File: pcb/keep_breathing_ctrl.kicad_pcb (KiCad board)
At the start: 4 copper layers, 131 x 112 mm, 177 parts, among them J2 Screw_Terminal, P1 CONN_RASPBERRY, Q1 PN2222, Q2 PN2222, U1 MPL3115A2, U10 PCF8523TK, U11 AQH3213AX, U12 AQH3213AX, U13 HTS221, U14 ICE40UP5K-SG48ITR, U15 GD25Q32CTIGR-Memory_Flash, U16 UCC12040, U17 ISO7762, U18 ZLDO1117G33TA, U19 NCP177, U2 powerSTEP01, U3 TLP240D, U4 TLP240D, U5 TLP240D, U6 TLP240D, U7 TLP240D, U8 TLP240D, U9 ZLDO1117G33TA, Y1 ABS06-107-32.768KHZ-T

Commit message: fix
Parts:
- moved C65 9.49 mm to (157.5, 103.0), turned to 180 degrees
- moved C67 3.77 mm to (157.5, 105.5), turned to 180 degrees
- moved C56 3.71 mm to (104.0, 107.0)
- moved C22 3.42 mm to (82.0, 114.0)
- moved C14 2.99 mm to (80.0, 121.5)
- moved C66 1.28 mm to (138.0, 107.0), turned to 180 degrees
- moved C64 0.89 mm to (134.0, 107.0)
- moved C57 0.46 mm to (108.0, 107.0), turned to 180 degrees
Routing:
- net +5V: track 83.5 -> 100.4 mm
- net +3V3: track 38.5 -> 48.5 mm

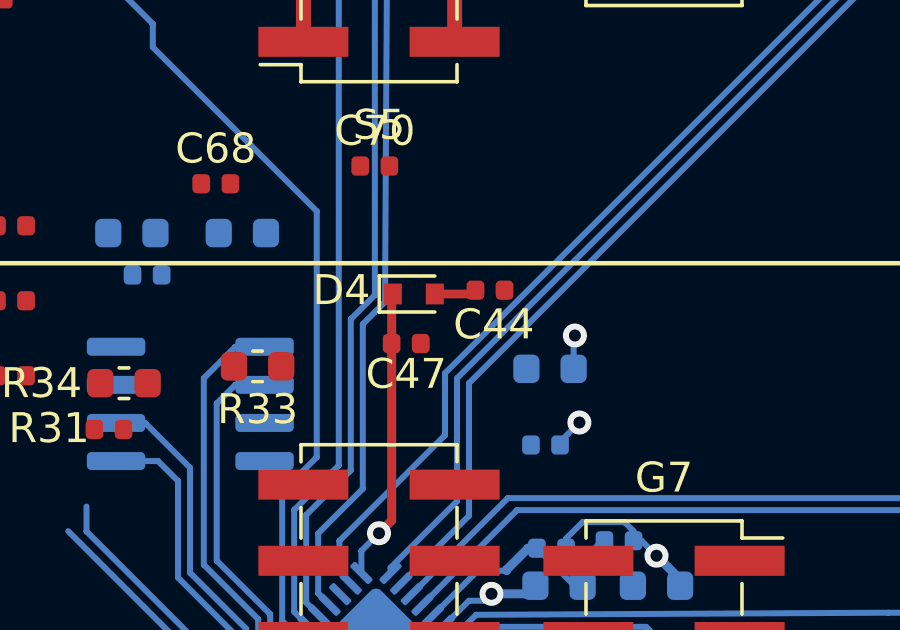
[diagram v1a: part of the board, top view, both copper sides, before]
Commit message: footprint fix
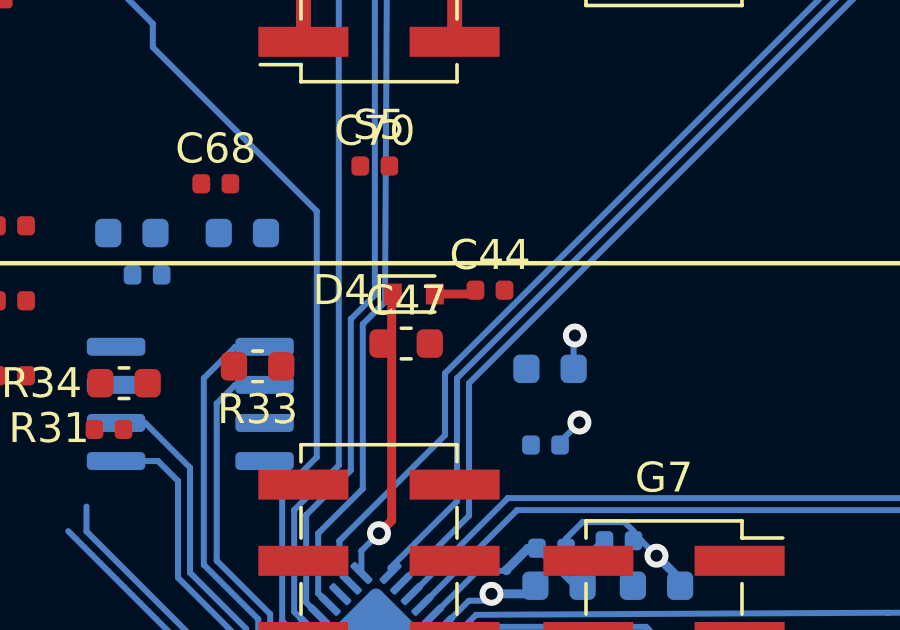
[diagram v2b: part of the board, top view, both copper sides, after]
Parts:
- C42, C44: footprint Resistor_SMD:R_0402_1005Metric -> Capacitor_SMD:C_0402_1005Metric
- C47: footprint Resistor_SMD:R_0402_1005Metric -> Capacitor_SMD:C_0603_1608Metric

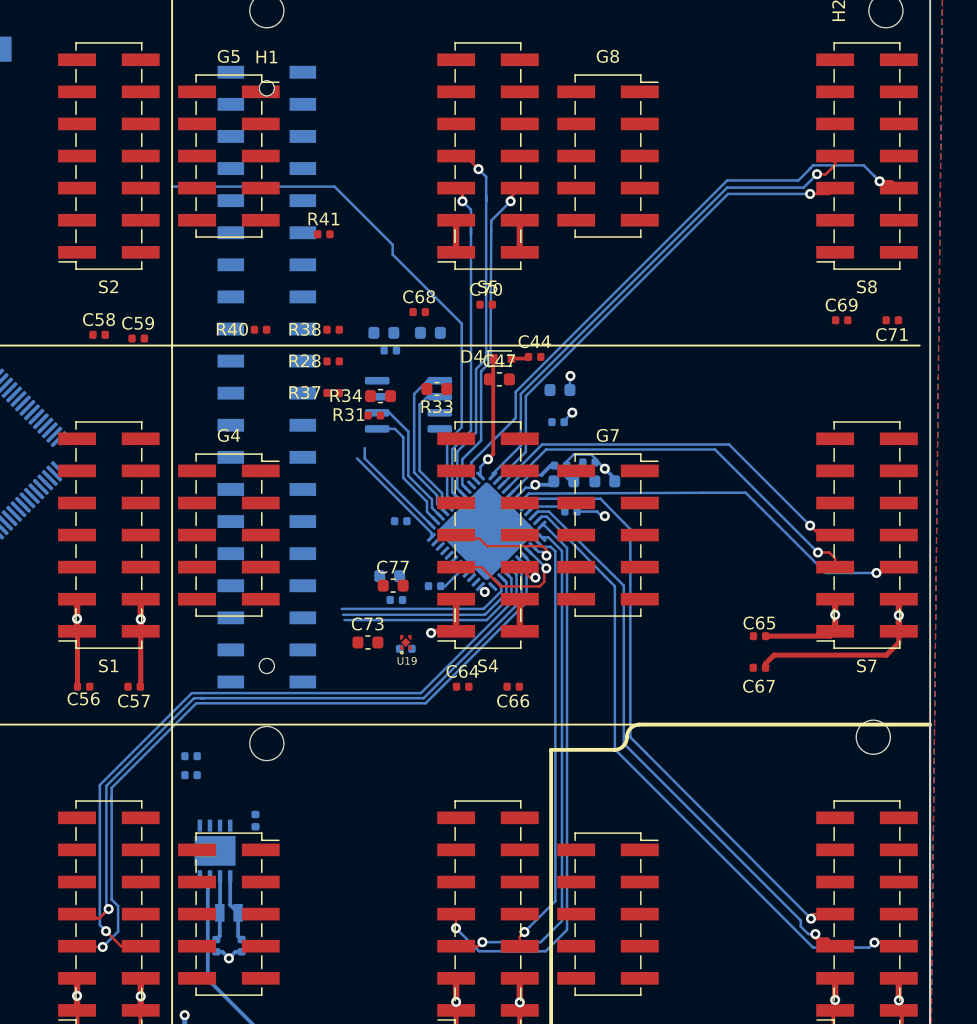
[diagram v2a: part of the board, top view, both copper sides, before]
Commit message: SPI for sensor shield array
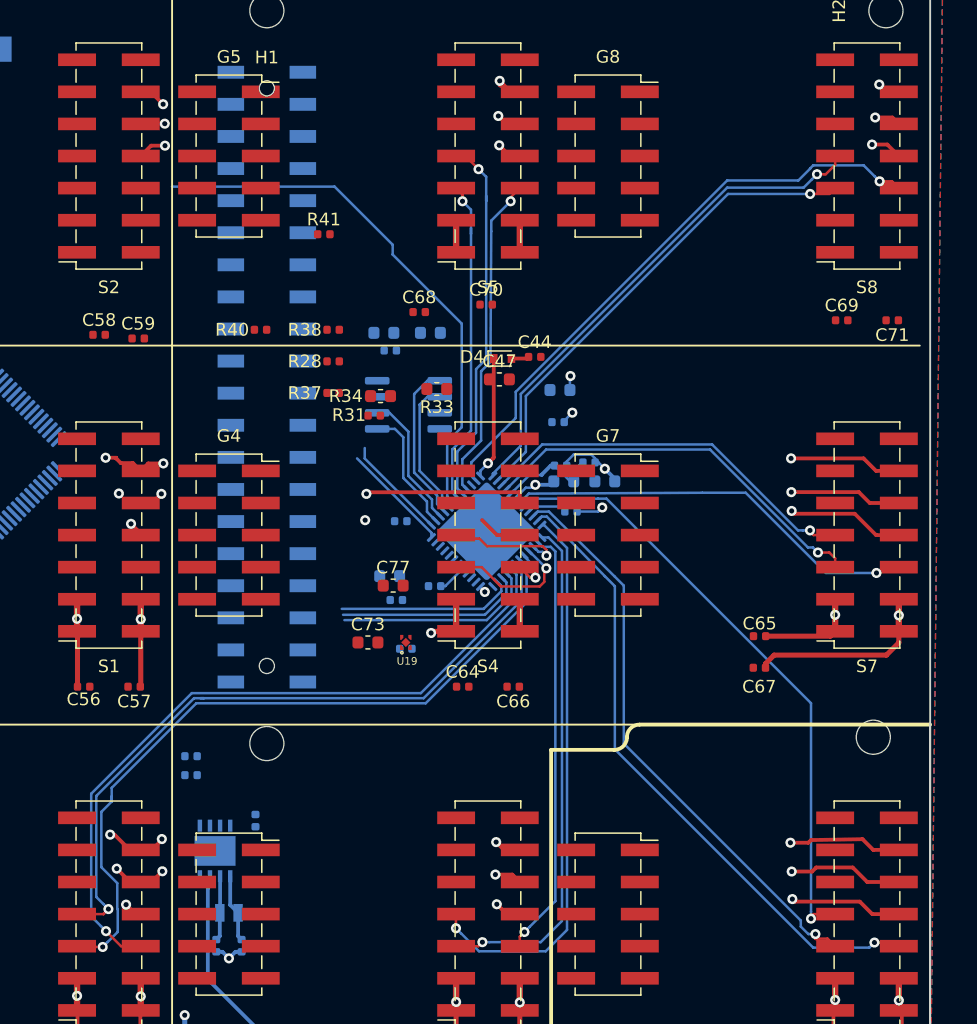
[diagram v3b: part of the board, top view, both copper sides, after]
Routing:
- net /SensorShields/SPI_MISO: track 0.00 -> 263.9 mm, vias 0 -> 11
- net /SensorShields/SPI_CLK: track 0.00 -> 256.8 mm, vias 0 -> 9
- net /SensorShields/SPI_MOSI: track 0.00 -> 254.5 mm, vias 0 -> 10
- net /SensorShields/I2C_CLK_0: track 58.3 -> 59.0 mm
- net /SensorShields/SPI_CS_0: track 56.6 -> 57.2 mm

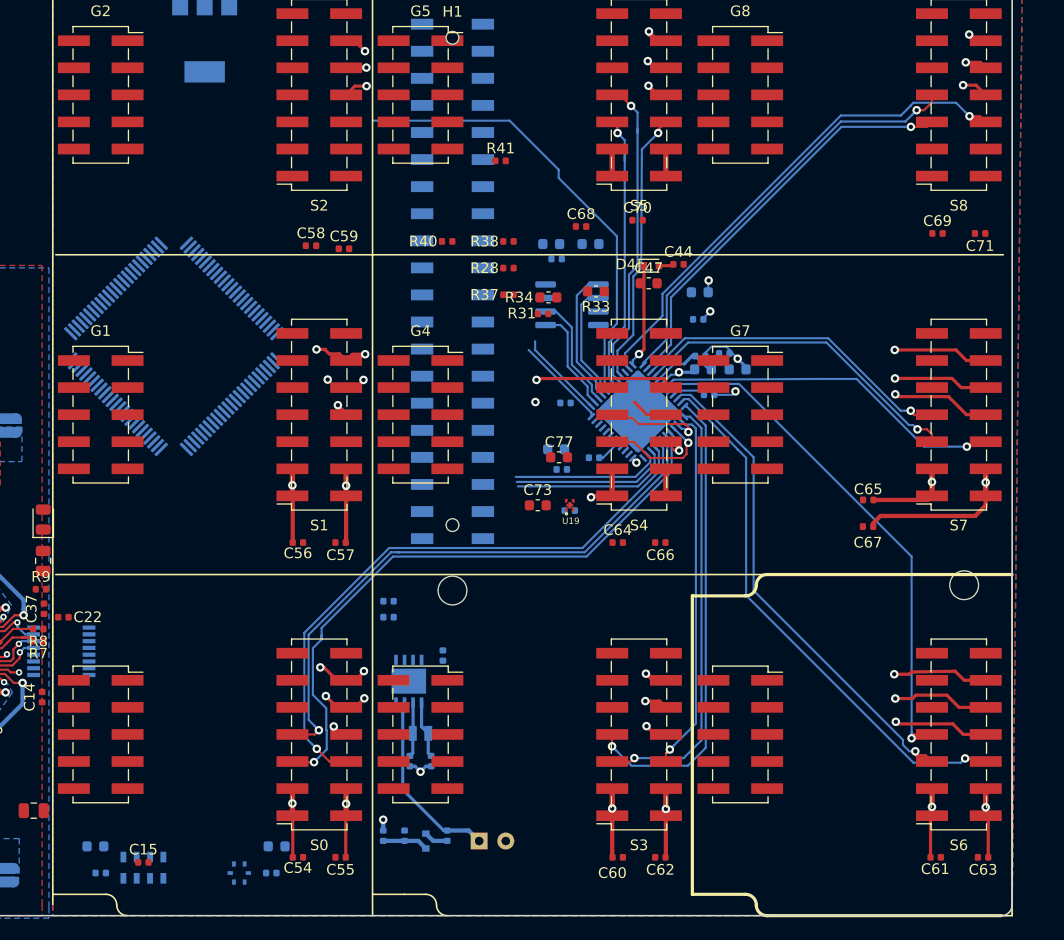
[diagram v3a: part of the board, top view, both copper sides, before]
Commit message: routing analog signals
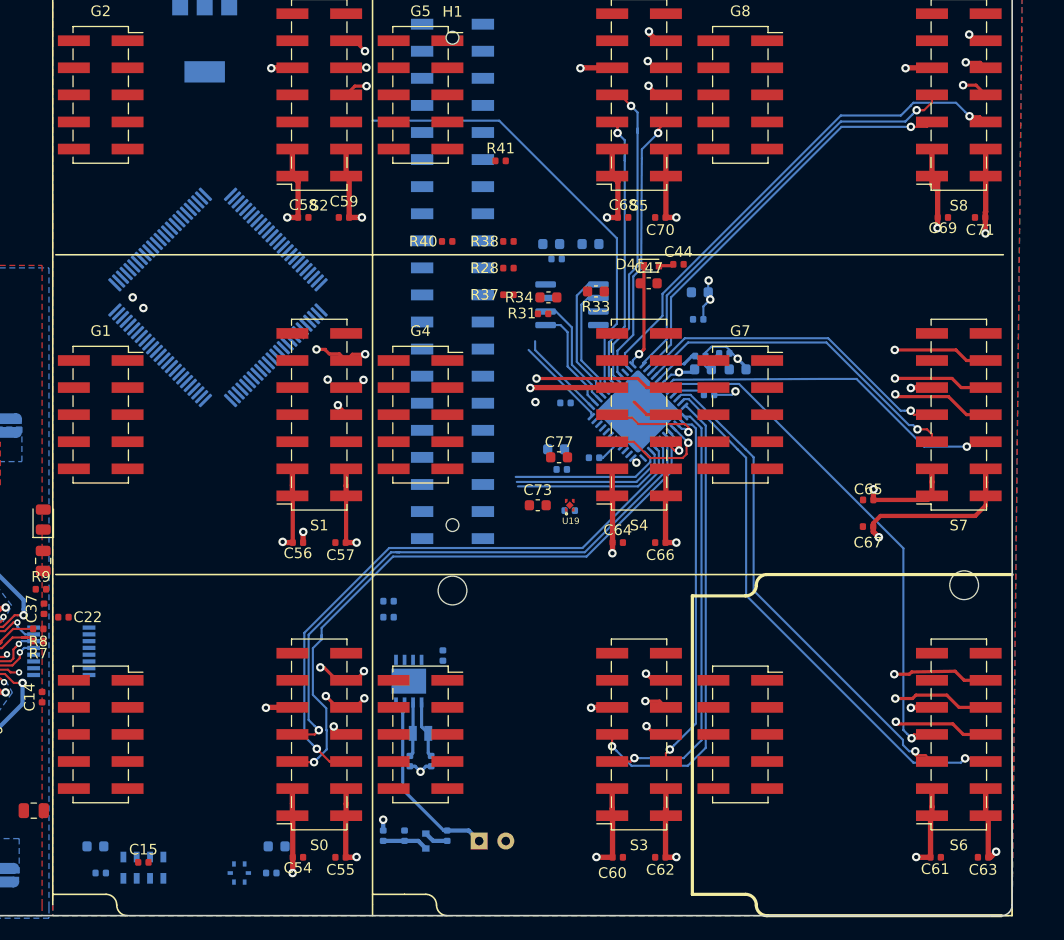
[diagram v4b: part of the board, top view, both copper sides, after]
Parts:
- moved UST1 6.18 mm to (96.5, 84.0)
- moved C68 4.03 mm to (134.5, 76.5)
- moved C59 2.94 mm to (108.3, 76.5), turned to 180 degrees
- moved C58 2.75 mm to (104.5, 76.5)
- moved C70 2.16 mm to (138.0, 76.5), turned to 180 degrees
- moved C69 1.58 mm to (164.5, 76.5)
- moved C71 1.50 mm to (168.0, 76.5)
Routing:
- net /SensorShields/ANALOG_6: track 0.00 -> 100.6 mm, vias 0 -> 1
- net /SensorShields/ANALOG_8: track 0.00 -> 75.0 mm, vias 0 -> 1
- net /SensorShields/ANALOG_7: track 0.00 -> 73.9 mm, vias 0 -> 1
- net /SensorShields/ANALOG_3: track 0.00 -> 71.8 mm, vias 0 -> 2
- net /SensorShields/ANALOG_0: track 0.00 -> 44.8 mm, vias 0 -> 2
- net /SensorShields/ANALOG_4: track 0.00 -> 44.1 mm, vias 0 -> 1
- net /SensorShields/ANALOG_5: track 0.00 -> 43.0 mm, vias 0 -> 1
- net +5V: track 100.4 -> 132.2 mm, vias 6 -> 10
- net +3V3: track 48.5 -> 78.7 mm, vias 7 -> 10
- net /SensorShields/ANALOG_2: track 0.00 -> 15.8 mm, vias 0 -> 1
- net GND: track 12.2 -> 14.4 mm, vias 5 -> 6
- net /SensorShields/SPI_CS_2: track 42.8 -> 42.2 mm

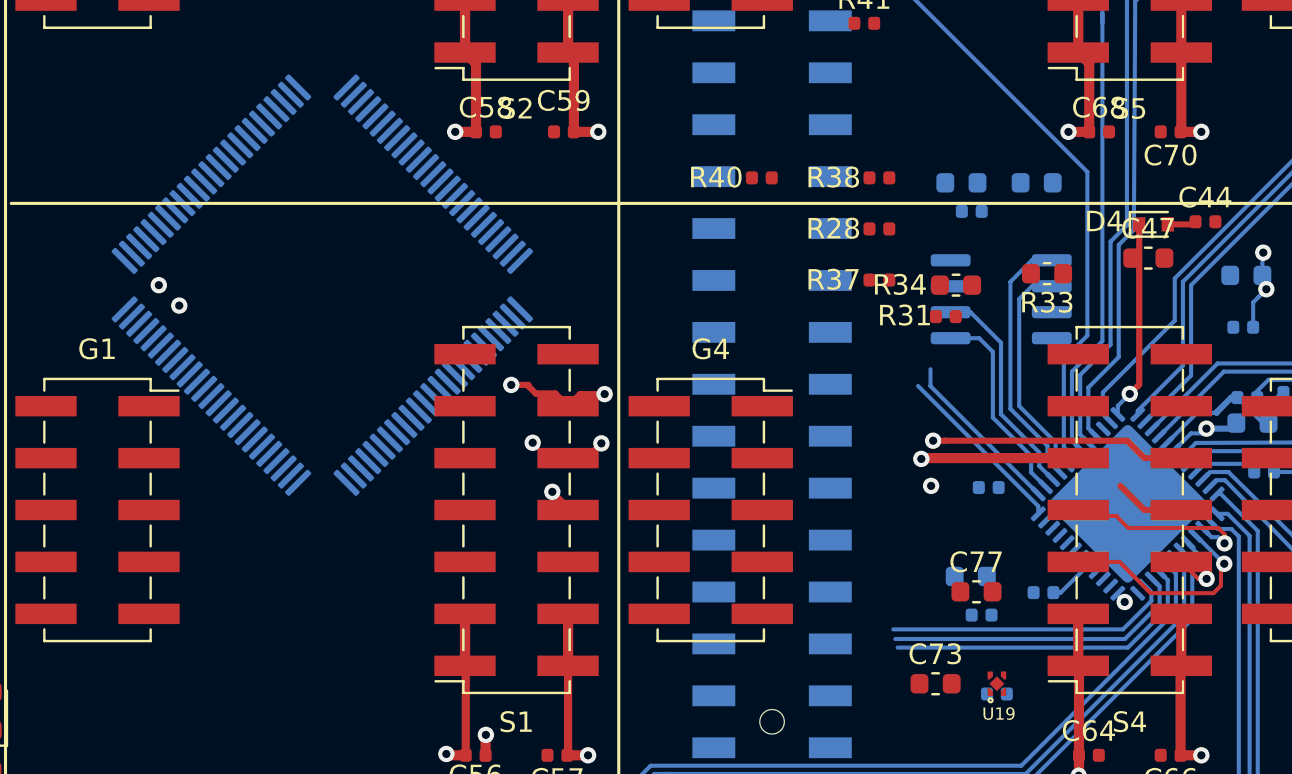
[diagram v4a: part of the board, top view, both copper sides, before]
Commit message: analog signals routed
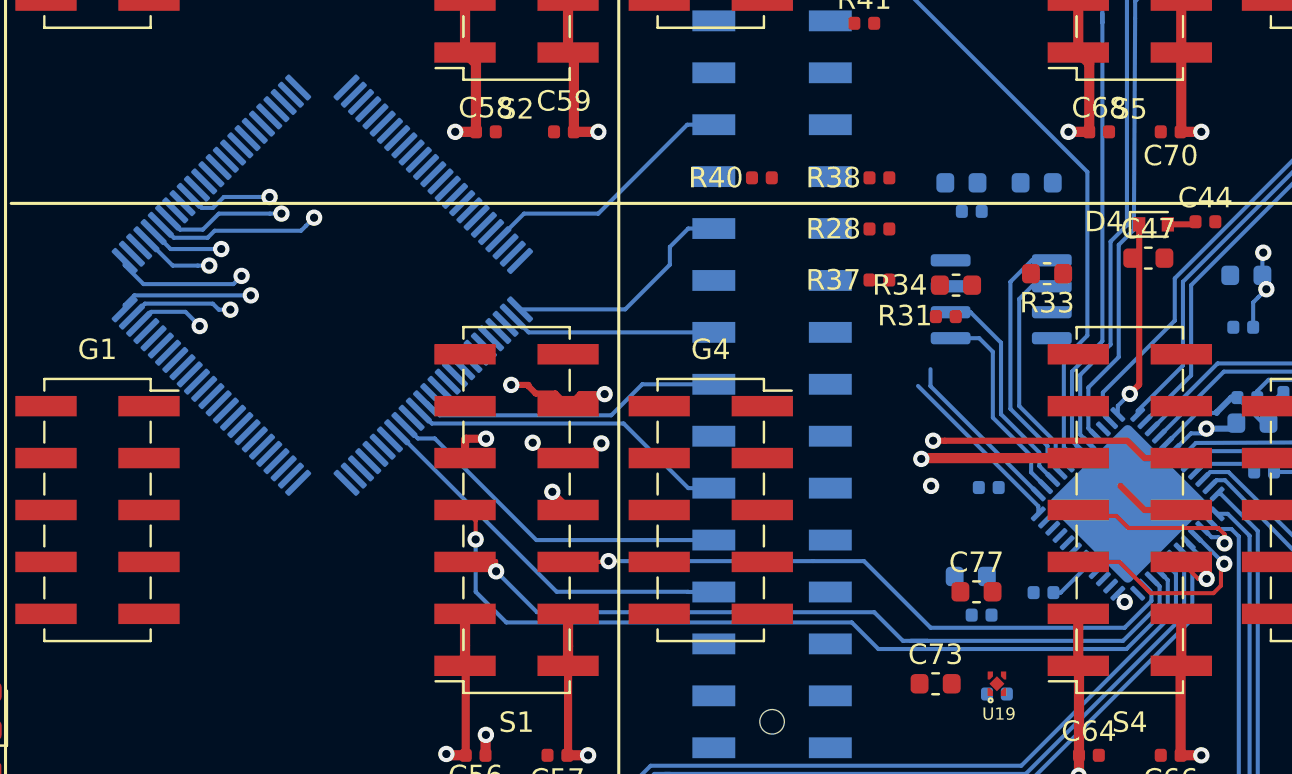
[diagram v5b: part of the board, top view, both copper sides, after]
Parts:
- UST1: value STM32F4_LQFP100 -> STM32F427VIT6
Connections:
- UST1 pad 24: /SensorShields/ANALOG_1 -> /SensorShields/ANALOG_3
- UST1 pad 25: /SensorShields/ANALOG_2 -> /SensorShields/ANALOG_6
- UST1 pad 26: /SensorShields/ANALOG_3 -> /SensorShields/ANALOG_1
- UST1 pad 30: /SensorShields/ANALOG_5 -> /SensorShields/ANALOG_7
- UST1 pad 31: /SensorShields/ANALOG_6 -> /SensorShields/ANALOG_8
- UST1 pad 32: /SensorShields/ANALOG_7 -> /SensorShields/ANALOG_5
- UST1 pad 35: /SensorShields/ANALOG_8 -> /SensorShields/ANALOG_2
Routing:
- net /SensorShields/I2C_SDA_1: track 16.0 -> 42.0 mm, vias 0 -> 1
- net /SensorShields/I2C_CLK_1: track 15.0 -> 38.9 mm, vias 0 -> 1
- net /SensorShields/ANALOG_1: track 0.00 -> 23.7 mm, vias 0 -> 2
- net /STM32F4/STM_UART_RX: track 0.00 -> 18.7 mm
- net /Rapsberry/RX_PI: track 0.00 -> 17.5 mm
- net /SensorShields/SPI_CS_1: track 14.1 -> 31.3 mm, vias 0 -> 1
- net /Rapsberry/JNRST: track 0.00 -> 16.0 mm
- net /Rapsberry/JTDO: track 0.00 -> 14.9 mm
- net /Rapsberry/JTMS: track 0.00 -> 12.9 mm
- net /Rapsberry/JTCK: track 0.00 -> 11.5 mm
- net /SensorShields/ANALOG_2: track 15.8 -> 27.0 mm, vias 1 -> 2
- net /Rapsberry/JTDI: track 0.00 -> 10.2 mm
- net /SensorShields/ANALOG_5: track 43.0 -> 52.6 mm, vias 1 -> 2
- net /SensorShields/ANALOG_7: track 73.9 -> 82.7 mm, vias 1 -> 2
- net /SensorShields/ANALOG_8: track 75.0 -> 83.1 mm, vias 1 -> 2
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
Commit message: routing...
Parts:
- moved C49 5.07 mm to (136.5, 86.6), turned to 45 degrees
- moved C51 4.74 mm to (137.0, 83.5), turned to 90 degrees
- moved R14 1.58 mm to (112.0, 115.5)
- moved R15 1.12 mm to (112.0, 113.5)
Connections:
- R14 pad 2: +5V -> +3V3
- R15 pad 2: +5V -> +3V3
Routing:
- net /I2C/I2C_SCL: track 0.00 -> 25.0 mm, vias 0 -> 2
- net /Rapsberry/INT_RTC: track 0.00 -> 24.9 mm, vias 0 -> 2
- net /I2C/I2C_SDA: track 0.00 -> 23.0 mm, vias 0 -> 2
- net +3V3: track 78.7 -> 101.2 mm, vias 10 -> 16
- net /SensorShields/SPI_CLK: track 256.8 -> 266.6 mm
- net /SensorShields/SPI_MOSI: track 254.4 -> 259.4 mm, vias 10 -> 11
- net GND: track 14.4 -> 18.6 mm, vias 6 -> 8
- net /SensorShields/I2C_CLK_8: track 38.9 -> 36.5 mm
- net /SensorShields/I2C_SDA_8: track 40.5 -> 38.1 mm
- net /SensorShields/SPI_MISO: track 264.3 -> 266.6 mm
- net +2V5: track 9.73 -> 11.5 mm
- net /SensorShields/SPI_CS_8: track 47.1 -> 45.7 mm
- net /SensorShields/I2C_SDA_5: track 29.7 -> 29.0 mm
- net /SensorShields/SPI_CS_7: track 33.1 -> 32.6 mm
- net /SensorShields/ANALOG_1: track 23.7 -> 23.2 mm

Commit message: rotate
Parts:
- moved C10 107.9 mm to (76.9, 31.5), turned to 270 degrees
- moved U8 106.4 mm to (168.6, 48.8), turned to 90 degrees
- moved D3 104.0 mm to (130.3, 27.7), turned to 180 degrees
- moved J2 102.7 mm to (86.9, 31.1), turned to 0 degrees
- moved H2 100.9 mm to (158.0, 154.0), turned to 0 degrees
- moved C27 100.9 mm to (156.8, 43.1), turned to 90 degrees
- moved R21 100.1 mm to (163.7, 50.1), turned to 270 degrees
- moved R11 100.1 mm to (130.7, 30.6), turned to 270 degrees
- moved U7 99.2 mm to (168.6, 56.8), turned to 90 degrees
- moved R26 97.4 mm to (152.4, 42.9), turned to 0 degrees
- moved C11 96.6 mm to (122.9, 31.5), turned to 270 degrees
- moved U11 96.4 mm to (155.5, 46.1), turned to 90 degrees
- moved C63 95.1 mm to (75.0, 154.8), turned to 90 degrees
- moved Q1 94.5 mm to (158.7, 50.7), turned to 180 degrees
- moved U6 92.8 mm to (168.6, 64.8), turned to 90 degrees
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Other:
- board size 131 x 112 mm -> 112 x 131 mm
